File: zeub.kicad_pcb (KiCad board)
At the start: 2 copper layers, 177.8 x 60 mm, 424 parts, among them J1 debug-port, J2 OLED-128x32, J3 USB_C_Receptacle_USB2.0, J4 Barrel_Jack_Switch, J5 Conn_01x03, J6 Conn_01x03, Q1 AO3401A, Q2 AO3401A, Q3 AO3401A, Q4 AO3401A, Q5 AO3401A, SW1 SKRHA, SW2 RotaryEncoder_Switch, U1 IS31FL3729, U10 LTC4054ES5-4.2, U2 IS31FL3729, U3 IS31FL3729, U4 IS31FL3729, U5 holyiot-18010-no-underside, U6 MT25QL128ABA1ESE, U7 TLV1117-50, U8 XC6206PxxxMR, U9 SRV05-4

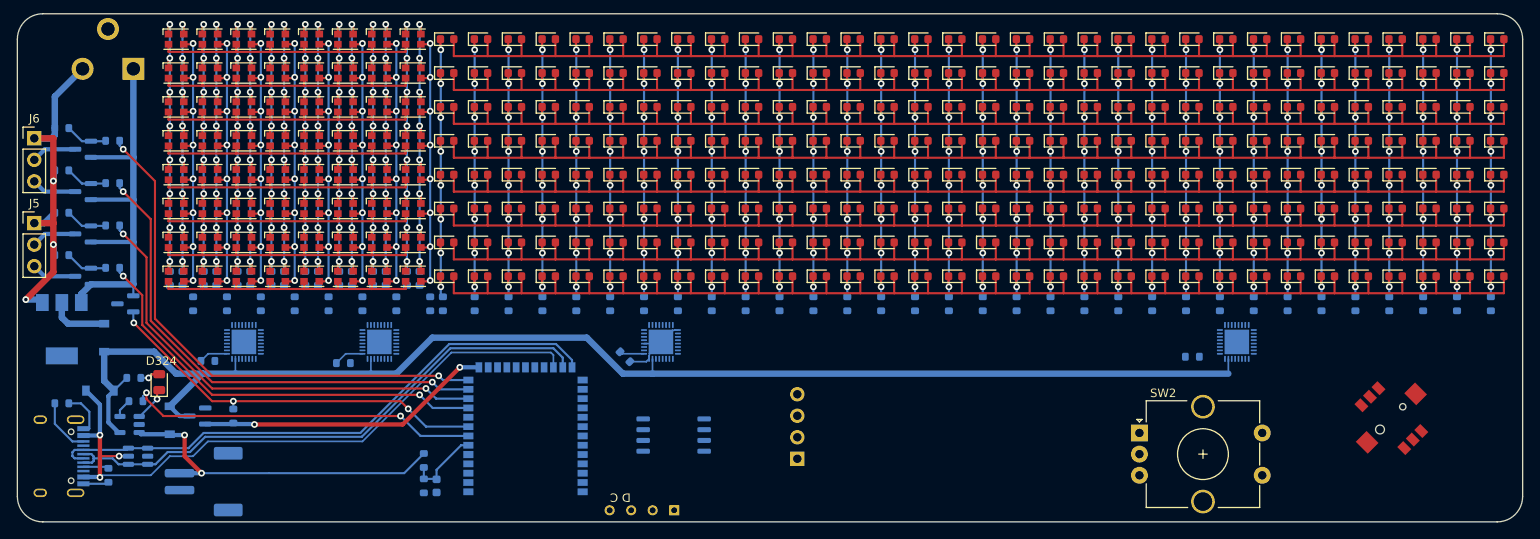
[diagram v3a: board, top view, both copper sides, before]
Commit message: routed PMU + rull RGB
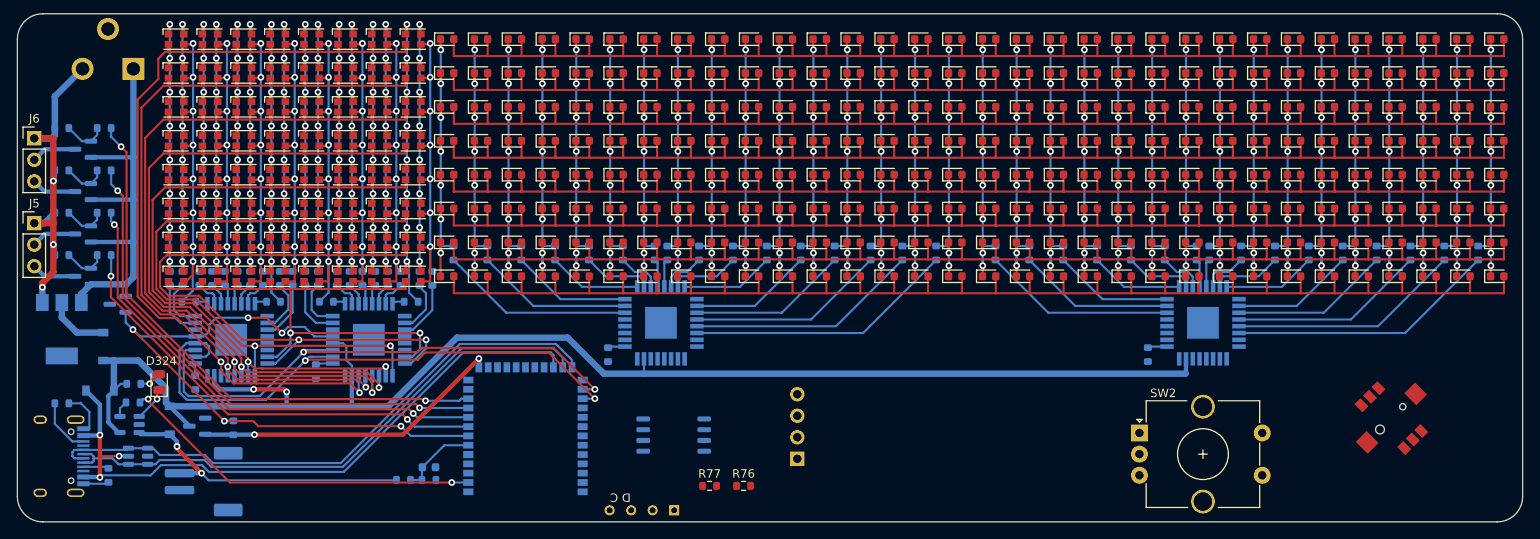
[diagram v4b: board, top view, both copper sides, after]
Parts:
- added R76: 2.2k, Resistor_SMD:R_0603_1608Metric, F.Cu at (67.0, 52.8)
- added R77: 2.2k, Resistor_SMD:R_0603_1608Metric, F.Cu at (63.0, 52.8)
- U1, U2, U3, U4: footprint Package_DFN_QFN:QFN-32-1EP_4x4mm_P0.4mm_EP2.9x2.9mm -> misc:eTQFP-32_7x7mm_P0.8mm
- moved R18 6.18 mm to (36.8, 25.2)
- moved R19 6.18 mm to (40.8, 25.2)
- moved R20 6.18 mm to (44.8, 25.2)
- moved R21 6.18 mm to (48.8, 25.2)
- moved R22 6.18 mm to (52.8, 25.2)
- moved R25 6.18 mm to (61.8, 25.2)
- moved R26 6.18 mm to (65.8, 25.2)
- moved R27 6.18 mm to (69.8, 25.2)
- moved R28 6.18 mm to (73.8, 25.2)
- moved R29 6.18 mm to (77.8, 25.2)
- moved R31 6.18 mm to (85.8, 25.2)
- moved R32 6.18 mm to (89.8, 25.2)
- moved R33 6.18 mm to (96.8, 25.2)
- moved R34 6.18 mm to (100.8, 25.2)
- moved R35 6.18 mm to (104.8, 25.2)
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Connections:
- R49 pad 1: Net-(U3-Pad30) -> Net-(R49-Pad1)
- R50 pad 1: Net-(U3-Pad31) -> Net-(R50-Pad1)
- R51 pad 1: Net-(U3-Pad32) -> Net-(R51-Pad1)
- R52 pad 1: Net-(U3-Pad1) -> Net-(U3-Pad2)
- R53 pad 1: Net-(U3-Pad2) -> Net-(U3-Pad3)
- R54 pad 1: Net-(U3-Pad3) -> Net-(U3-Pad4)
- R55 pad 1: Net-(U3-Pad4) -> Net-(U3-Pad5)
- R56 pad 1: Net-(U3-Pad5) -> Net-(U3-Pad6)
- R57 pad 1: Net-(U3-Pad6) -> Net-(R57-Pad1)
- R58 pad 1: Net-(U3-Pad7) -> Net-(R58-Pad1)
- R59 pad 1: Net-(U3-Pad8) -> Net-(R59-Pad1)
- R60 pad 1: Net-(U3-Pad10) -> Net-(R60-Pad1)
- R61 pad 1: Net-(U4-Pad30) -> Net-(R61-Pad1)
- R62 pad 1: Net-(U4-Pad31) -> Net-(R62-Pad1)
- R63 pad 1: Net-(U4-Pad32) -> Net-(R63-Pad1)
- R64 pad 1: Net-(U4-Pad1) -> Net-(R64-Pad1)
- R65 pad 1: Net-(U4-Pad2) -> Net-(R65-Pad1)
- R66 pad 1: Net-(U4-Pad3) -> Net-(R66-Pad1)
- R67 pad 1: Net-(U4-Pad4) -> Net-(R67-Pad1)
- R68 pad 1: Net-(U4-Pad5) -> Net-(R68-Pad1)
- R69 pad 1: Net-(U4-Pad6) -> Net-(R69-Pad1)
- R70 pad 1: Net-(U4-Pad7) -> Net-(R70-Pad1)
- R71 pad 1: Net-(U4-Pad8) -> Net-(R71-Pad1)
- R72 pad 1: Net-(U4-Pad10) -> Net-(U4-Pad11)
- U1 pad 29: /led/~{SHDN} -> HAS_12V
- U2 pad 29: /led/~{SHDN} -> HAS_12V
- U3 pad 1: Net-(U3-Pad1) -> Net-(R51-Pad1)
- U3 pad 10: Net-(U3-Pad10) -> Net-(R59-Pad1)
- U3 pad 11: unconnected-(U3-Pad11) -> Net-(R60-Pad1)
- U3 pad 15: /led/RGB_C0 -> /led/RGB_C7
- U3 pad 16: /led/RGB_C1 -> /led/RGB_C6
- U3 pad 17: /led/RGB_C2 -> /led/RGB_C5
- U3 pad 18: /led/RGB_C3 -> /led/RGB_C4
- U3 pad 19: /led/RGB_C4 -> /led/RGB_C3
- U3 pad 20: /led/RGB_C5 -> /led/RGB_C2
- U3 pad 21: /led/RGB_C6 -> /led/RGB_C1
- U3 pad 22: /led/RGB_C7 -> /led/RGB_C0
- U3 pad 29: /led/~{SHDN} -> HAS_12V
- U3 pad 30: Net-(U3-Pad30) -> unconnected-(U3-Pad30)
- U3 pad 31: Net-(U3-Pad31) -> Net-(R49-Pad1)
- U3 pad 32: Net-(U3-Pad32) -> Net-(R50-Pad1)
- U3 pad 7: Net-(U3-Pad7) -> Net-(R57-Pad1)
- U3 pad 8: Net-(U3-Pad8) -> Net-(R58-Pad1)
- U4 pad 1: Net-(U4-Pad1) -> Net-(R63-Pad1)
- U4 pad 10: Net-(U4-Pad10) -> Net-(R71-Pad1)
- U4 pad 11: unconnected-(U4-Pad11) -> Net-(U4-Pad11)
- U4 pad 15: /led/RGB_C0 -> /led/RGB_C7
- U4 pad 16: /led/RGB_C1 -> /led/RGB_C6
- U4 pad 17: /led/RGB_C2 -> /led/RGB_C5
- U4 pad 18: /led/RGB_C3 -> /led/RGB_C4
- U4 pad 19: /led/RGB_C4 -> /led/RGB_C3
- U4 pad 2: Net-(U4-Pad2) -> Net-(R64-Pad1)
- U4 pad 20: /led/RGB_C5 -> /led/RGB_C2
- U4 pad 21: /led/RGB_C6 -> /led/RGB_C1
- U4 pad 22: /led/RGB_C7 -> /led/RGB_C0
- U4 pad 29: /led/~{SHDN} -> HAS_12V
- U4 pad 3: Net-(U4-Pad3) -> Net-(R65-Pad1)
- U4 pad 30: Net-(U4-Pad30) -> unconnected-(U4-Pad30)
- U4 pad 31: Net-(U4-Pad31) -> Net-(R61-Pad1)
- U4 pad 32: Net-(U4-Pad32) -> Net-(R62-Pad1)
- U4 pad 4: Net-(U4-Pad4) -> Net-(R66-Pad1)
- U4 pad 5: Net-(U4-Pad5) -> Net-(R67-Pad1)
- U4 pad 6: Net-(U4-Pad6) -> Net-(R68-Pad1)
- U4 pad 7: Net-(U4-Pad7) -> Net-(R69-Pad1)
- U4 pad 8: Net-(U4-Pad8) -> Net-(R70-Pad1)
- U5 pad 10: PWMY1 -> PWMY0
- U5 pad 11: PWMW1 -> PWMW0
- U5 pad 12: PWMY0 -> unconnected-(U5-Pad12)
- U5 pad 13: PWMW0 -> unconnected-(U5-Pad13)
- U5 pad 2: unconnected-(U5-Pad2) -> ~{CHG}
- U5 pad 42: SCL -> SDA
- U5 pad 43: SDA -> SCL
- U5 pad 7: ~{CHG} -> HAS_12V
- U5 pad 8: HAS_12V -> PWMY1
- U5 pad 9: unconnected-(U5-Pad9) -> PWMW1
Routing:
- net SDA: track 0.00 -> 70.5 mm, vias 0 -> 2
- net /led/RGB_C0: track 35.2 -> 101.1 mm, vias 0 -> 2
- net SCL: track 0.00 -> 64.2 mm, vias 0 -> 2
- net /led/RGB_C1: track 35.2 -> 95.9 mm, vias 0 -> 2
- net /led/RGB_C2: track 35.2 -> 93.9 mm, vias 0 -> 2
- net /led/RGB_C3: track 35.2 -> 88.0 mm, vias 0 -> 2
- net /led/RGB_C4: track 35.2 -> 82.8 mm, vias 0 -> 2
- net /led/RGB_C6: track 35.2 -> 82.7 mm, vias 0 -> 2
- net /led/RGB_C5: track 35.2 -> 81.5 mm, vias 0 -> 2
- net Net-(R48-Pad1): track 0.00 -> 31.8 mm
- net Net-(R32-Pad1): track 0.00 -> 31.8 mm
- net /led/RGB_C7: track 35.2 -> 65.4 mm, vias 0 -> 2
- net HAS_12V: track 46.8 -> 75.1 mm, vias 3 -> 5
- net Net-(R47-Pad1): track 0.00 -> 27.5 mm
- net Net-(R31-Pad1): track 0.00 -> 27.5 mm
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
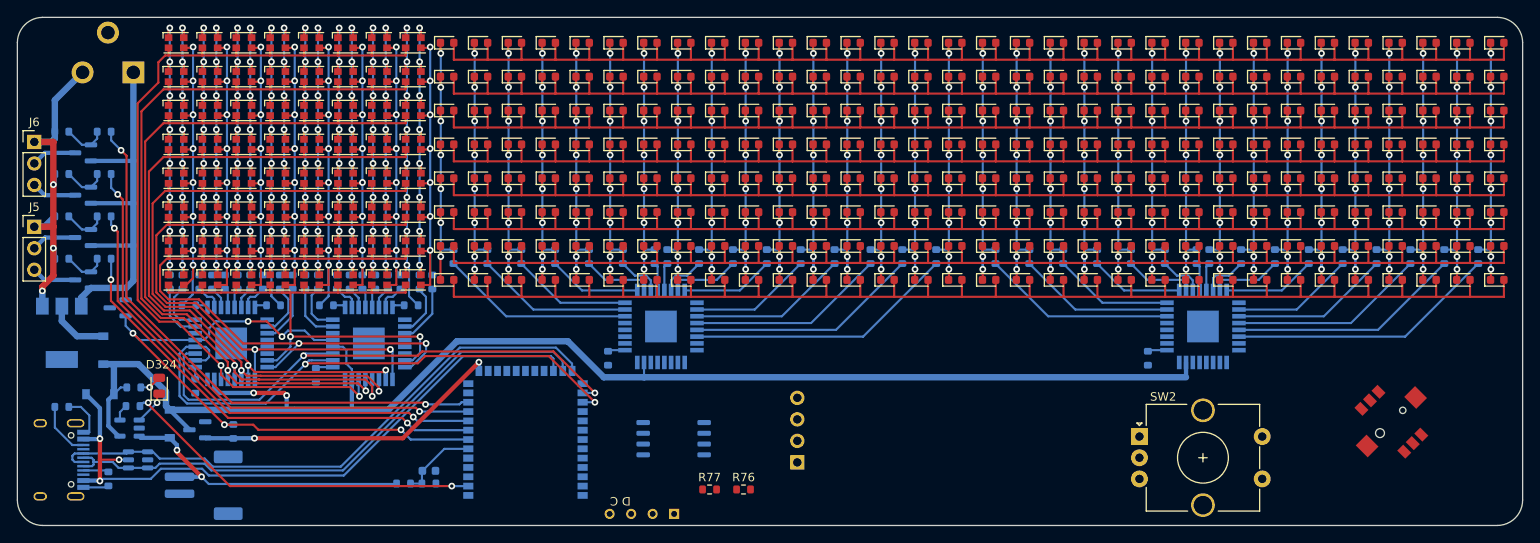
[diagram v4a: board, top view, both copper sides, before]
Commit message: routed all LED + PMU
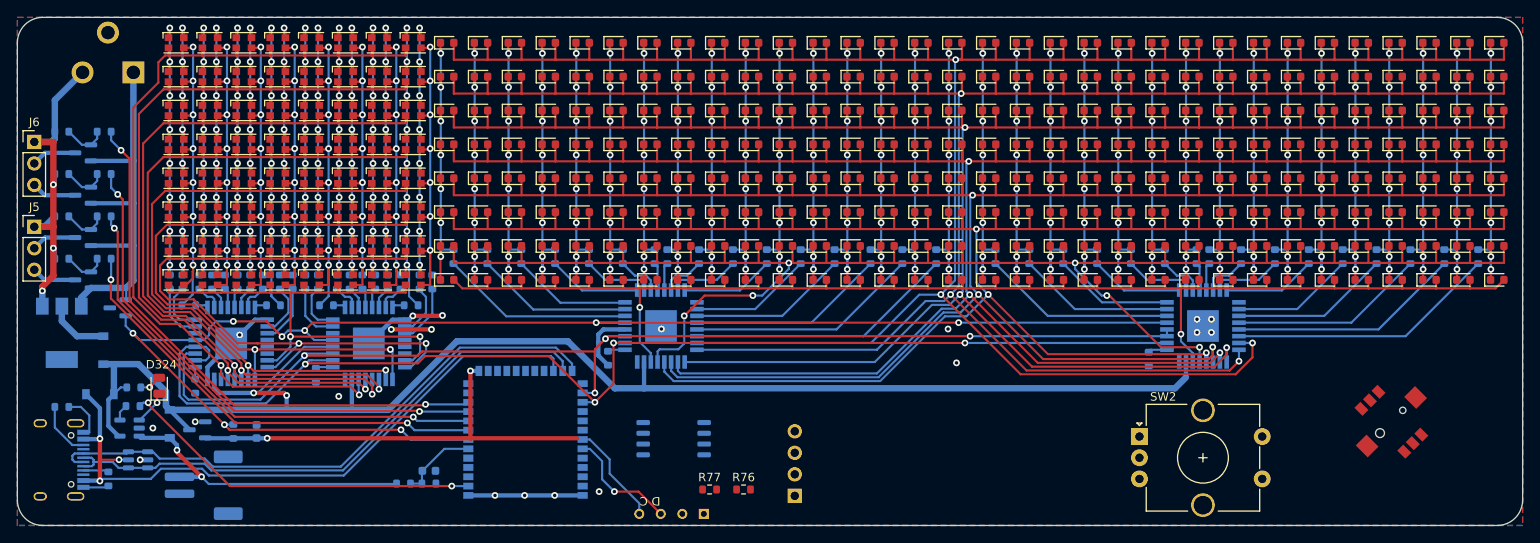
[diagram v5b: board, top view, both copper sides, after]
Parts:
- added C2: 1uF, Capacitor_SMD:C_0603_1608Metric, B.Cu at (9.50, 45.9)
- moved J2 3.96 mm to (71.5, 43.7)
- moved J1 3.50 mm to (58.5, 55.6)
- moved R14 0.14 mm to (114.8, 37.4)
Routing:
- net /led/W_R0: track 188.0 -> 293.9 mm, vias 0 -> 3
- net HAS_12V: track 75.1 -> 180.7 mm, vias 5 -> 8
- net /led/W_R1: track 188.0 -> 284.6 mm, vias 0 -> 3
- net /led/W_R2: track 188.0 -> 281.9 mm, vias 0 -> 3
- net /led/W_R3: track 188.0 -> 278.0 mm, vias 0 -> 3
- net /led/W_R4: track 188.0 -> 275.7 mm, vias 0 -> 3
- net /led/W_R5: track 188.0 -> 270.2 mm, vias 0 -> 3
- net SCL: track 64.2 -> 143.6 mm, vias 2 -> 4
- net SDA: track 70.5 -> 145.1 mm, vias 2 -> 4
- net GND: track 50.3 -> 97.0 mm, vias 3 -> 23
- net /led/W_R6: track 188.0 -> 232.4 mm, vias 0 -> 6
- net +3V3: track 37.1 -> 52.9 mm
- net /led/W_R7: track 188.0 -> 173.3 mm, vias 0 -> 2
- net SWD: track 0.00 -> 13.7 mm, vias 0 -> 1
- net SWC: track 0.00 -> 12.1 mm
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- added copper zone on B.Cu, net GND
- added copper zone on F.Cu, net GND

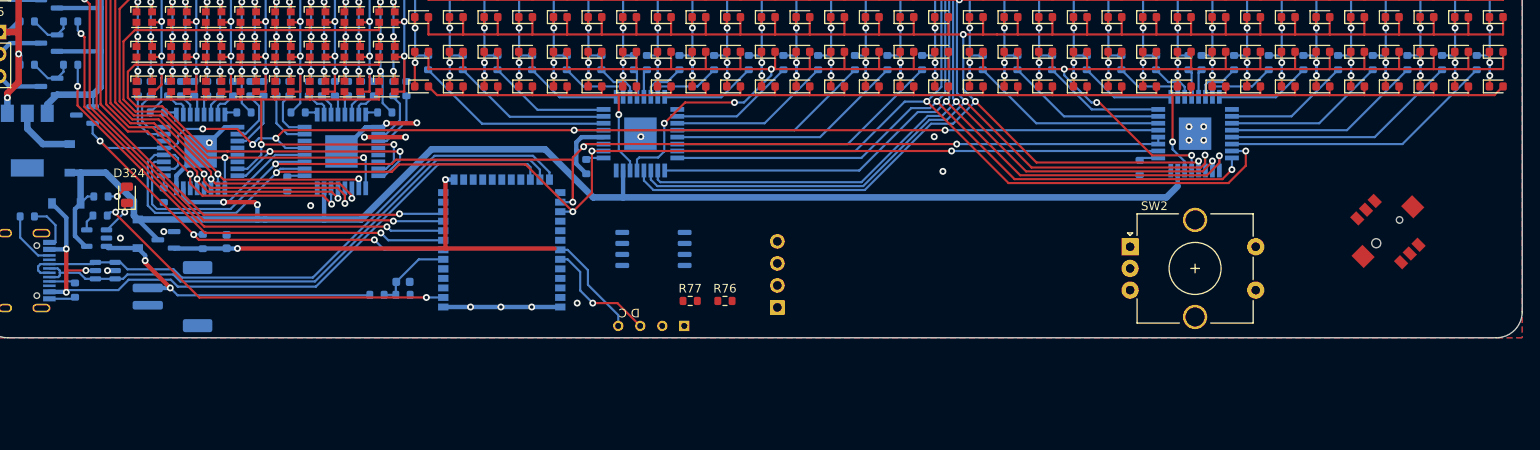
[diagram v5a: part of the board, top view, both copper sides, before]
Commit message: rid of LED driver resistors
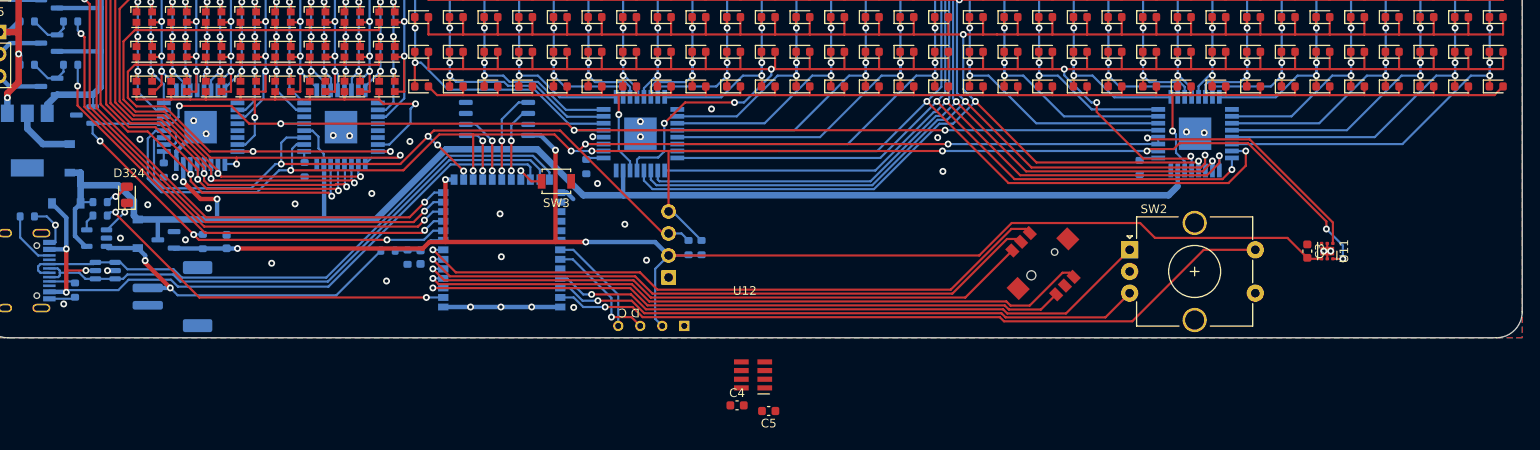
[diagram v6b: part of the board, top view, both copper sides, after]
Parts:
- removed R17, R18, R19, R20, R21, R22, R23, R24, R25, R26, R27, R28, R29, R30, R31, R32, R33, R34, R35, R36, R37, R38, R39, R40, R41, R42, R43, R44, R45, R46, R47, R48, R50, R51, R53, R54, R56, R57, R59, R60, R62, R63, R65, R66, R68, R69, R71, R72: 20, Resistor_SMD:R_0603_1608Metric
- removed R49, R52, R55, R58, R61, R64, R67, R70: 51, Resistor_SMD:R_0603_1608Metric
- added C3: 0.1uF, Capacitor_SMD:C_0603_1608Metric, F.Cu at (134.2, 47.0)
- added C4: 10uF, Capacitor_SMD:C_0603_1608Metric, F.Cu at (68.4, 64.8)
- added C5: 0.1uF, Capacitor_SMD:C_0603_1608Metric, F.Cu at (72.0, 65.5)
- added SW3: SW_Push, Button_Switch_SMD:SW_SPST_B3U-1000P, F.Cu at (47.5, 39.0)
- added U11: TMP117, Package_SON:WSON-6-1EP_2x2mm_P0.65mm_EP1x1.6mm, F.Cu at (136.5, 47.0)
- added U12: CMM4030D, ic:CMM4030D_hand_solder, F.Cu at (70.2, 61.3)
- R76, R77: moved to B.Cu
- moved SW1 40.0 mm to (103.7, 48.5)
- moved U6 23.5 mm to (40.7, 31.8), turned to 0 degrees
- moved J2 13.0 mm to (58.9, 40.2)
- moved R76 6.72 mm to (64.3, 46.6), turned to 90 degrees
- moved R77 6.15 mm to (62.8, 46.6), turned to 90 degrees
- moved R74 5.26 mm to (28.1, 47.0)
- moved R75 4.38 mm to (30.4, 47.7), turned to -90 degrees
- moved C1 3.50 mm to (31.9, 47.7), turned to -90 degrees
- moved R15 2.90 mm to (2.25, 37.6)
- moved U4 2.80 mm to (22.7, 32.7)
- moved U3 2.80 mm to (6.50, 32.7)
- moved R16 2.59 mm to (18.5, 37.6)
- moved R11 0.66 mm to (-5.10, 41.4)
- moved SW2 0.35 mm to (113.7, 46.9)
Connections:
- SW1 pad 1: unconnected-(SW1-Pad1) -> A
- SW1 pad 2: unconnected-(SW1-Pad2) -> E
- SW1 pad 3: unconnected-(SW1-Pad3) -> C
- SW1 pad 4: unconnected-(SW1-Pad4) -> B
- SW1 pad 5: unconnected-(SW1-Pad5) -> GND
- SW1 pad 6: unconnected-(SW1-Pad6) -> D
- SW2 pad A: unconnected-(SW2-PadA) -> ENC_A
- SW2 pad B: unconnected-(SW2-PadB) -> ENC_B
- SW2 pad C: unconnected-(SW2-PadC) -> GND
- SW2 pad S1: unconnected-(SW2-PadS1) -> ENC_PUSH
- SW2 pad S2: unconnected-(SW2-PadS2) -> GND
- U1 pad 1: Net-(R20-Pad1) -> /led/W_C03
- U1 pad 10: Net-(R28-Pad1) -> /led/W_C11
- U1 pad 11: Net-(R29-Pad1) -> /led/W_C12
- U1 pad 12: Net-(R30-Pad1) -> /led/W_C13
- U1 pad 13: Net-(R31-Pad1) -> /led/W_C14
- U1 pad 14: Net-(R32-Pad1) -> /led/W_C15
- U1 pad 2: Net-(R21-Pad1) -> /led/W_C04
- U1 pad 3: Net-(R22-Pad1) -> /led/W_C05
- U1 pad 30: Net-(R17-Pad1) -> /led/W_C00
- U1 pad 31: Net-(R18-Pad1) -> /led/W_C01
- U1 pad 32: Net-(R19-Pad1) -> /led/W_C02
- U1 pad 4: Net-(R23-Pad1) -> /led/W_C06
- U1 pad 5: Net-(R24-Pad1) -> /led/W_C07
- U1 pad 6: Net-(R25-Pad1) -> /led/W_C08
- U1 pad 7: Net-(R26-Pad1) -> /led/W_C09
- U1 pad 8: Net-(R27-Pad1) -> /led/W_C10
- U2 pad 1: Net-(R36-Pad1) -> /led/W_C19
- U2 pad 10: Net-(R44-Pad1) -> /led/W_C27
- U2 pad 11: Net-(R45-Pad1) -> /led/W_C28
- U2 pad 12: Net-(R46-Pad1) -> /led/W_C29
- U2 pad 13: Net-(R47-Pad1) -> /led/W_C30
- U2 pad 14: Net-(R48-Pad1) -> /led/W_C31
- U2 pad 2: Net-(R37-Pad1) -> /led/W_C20
- U2 pad 3: Net-(R38-Pad1) -> /led/W_C21
- U2 pad 30: Net-(R33-Pad1) -> /led/W_C16
- U2 pad 31: Net-(R34-Pad1) -> /led/W_C17
- U2 pad 32: Net-(R35-Pad1) -> /led/W_C18
- U2 pad 4: Net-(R39-Pad1) -> /led/W_C22
- U2 pad 5: Net-(R40-Pad1) -> /led/W_C23
- U2 pad 6: Net-(R41-Pad1) -> /led/W_C24
- U2 pad 7: Net-(R42-Pad1) -> /led/W_C25
- U2 pad 8: Net-(R43-Pad1) -> /led/W_C26
- U3 pad 1: Net-(R51-Pad1) -> /led/RGB_B0
- U3 pad 10: Net-(R59-Pad1) -> /led/RGB_G3
- U3 pad 11: Net-(R60-Pad1) -> /led/RGB_B3
- U3 pad 2: Net-(R52-Pad1) -> /led/RGB_R1
- U3 pad 3: Net-(R53-Pad1) -> /led/RGB_G1
- U3 pad 31: Net-(R49-Pad1) -> /led/RGB_R0
- U3 pad 32: Net-(R50-Pad1) -> /led/RGB_G0
- U3 pad 4: Net-(R54-Pad1) -> /led/RGB_B1
- U3 pad 5: Net-(R55-Pad1) -> /led/RGB_R2
- U3 pad 6: Net-(R56-Pad1) -> /led/RGB_G2
- U3 pad 7: Net-(R57-Pad1) -> /led/RGB_B2
- U3 pad 8: Net-(R58-Pad1) -> /led/RGB_R3
- U4 pad 1: Net-(R63-Pad1) -> /led/RGB_B4
- U4 pad 10: Net-(R71-Pad1) -> /led/RGB_G7
- U4 pad 11: Net-(R72-Pad1) -> /led/RGB_B7
- U4 pad 2: Net-(R64-Pad1) -> /led/RGB_R5
- U4 pad 3: Net-(R65-Pad1) -> /led/RGB_G5
- U4 pad 31: Net-(R61-Pad1) -> /led/RGB_R4
- U4 pad 32: Net-(R62-Pad1) -> /led/RGB_G4
- U4 pad 4: Net-(R66-Pad1) -> /led/RGB_B5
- U4 pad 5: Net-(R67-Pad1) -> /led/RGB_R6
- U4 pad 6: Net-(R68-Pad1) -> /led/RGB_G6
- U4 pad 7: Net-(R69-Pad1) -> /led/RGB_B6
- U4 pad 8: Net-(R70-Pad1) -> /led/RGB_R7
- U5 pad 10: PWMY0 -> PWMY1
- U5 pad 11: PWMW0 -> PWMW1
- U5 pad 12: unconnected-(U5-Pad12) -> PWMY0
- U5 pad 13: unconnected-(U5-Pad13) -> PWMW0
- U5 pad 3: unconnected-(U5-Pad3) -> D
- U5 pad 33: unconnected-(U5-Pad33) -> ENC_PUSH
- U5 pad 34: unconnected-(U5-Pad34) -> ENC_B
- U5 pad 35: unconnected-(U5-Pad35) -> ENC_A
- U5 pad 4: unconnected-(U5-Pad4) -> B
- U5 pad 42: SDA -> unconnected-(U5-Pad42)
- U5 pad 43: SCL -> unconnected-(U5-Pad43)
- U5 pad 48: unconnected-(U5-Pad48) -> Net-(SW3-Pad2)
- U5 pad 5: unconnected-(U5-Pad5) -> C
- U5 pad 53: unconnected-(U5-Pad53) -> SDA
- U5 pad 54: unconnected-(U5-Pad54) -> SCL
- U5 pad 6: BAT_MEAS -> E
- U5 pad 7: HAS_12V -> A
- U5 pad 8: PWMY1 -> BAT_MEAS
- U5 pad 9: PWMW1 -> HAS_12V
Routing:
- net +3V3: track 52.9 -> 172.2 mm, vias 2 -> 4
- net ENC_PUSH: track 0.00 -> 84.8 mm, vias 0 -> 1
- net B: track 0.00 -> 78.2 mm, vias 0 -> 1
- net A: track 0.00 -> 75.1 mm, vias 0 -> 1
- net D: track 0.00 -> 74.9 mm, vias 0 -> 1
- net E: track 0.00 -> 73.5 mm, vias 0 -> 1
- net C: track 0.00 -> 71.7 mm, vias 0 -> 1
- net ENC_A: track 0.00 -> 70.4 mm, vias 0 -> 1
- net ENC_B: track 0.00 -> 68.3 mm, vias 0 -> 1
- net SDA: track 145.1 -> 198.2 mm, vias 4 -> 8
- net SCL: track 143.6 -> 187.5 mm, vias 4 -> 7
- net Net-(R48-Pad1): track 31.8 -> 0.00 mm
- net Net-(R32-Pad1): track 31.8 -> 0.00 mm
- net /led/W_C31: track 39.4 -> 71.0 mm
- net /led/W_C15: track 39.4 -> 71.0 mm
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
